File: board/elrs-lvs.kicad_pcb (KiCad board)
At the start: 4 copper layers, 46 x 22 mm, 88 parts, among them J1 PWM, J10 CF/Prog, J12 Balance, J13 U.FL, J2 PWM, J3 PWM, J4 PWM, J5 PWM, J6 PWM, J7 PWM, J8 PWM, J9 Little Tower, SW1 SW_SPST, SW2 SW_SPST, U1 ESP32-PICO-V3, U2 SX1281, U3 TPSM82901SISR, U4 2450FM07D0034T, Y1 52Mhz TCXO

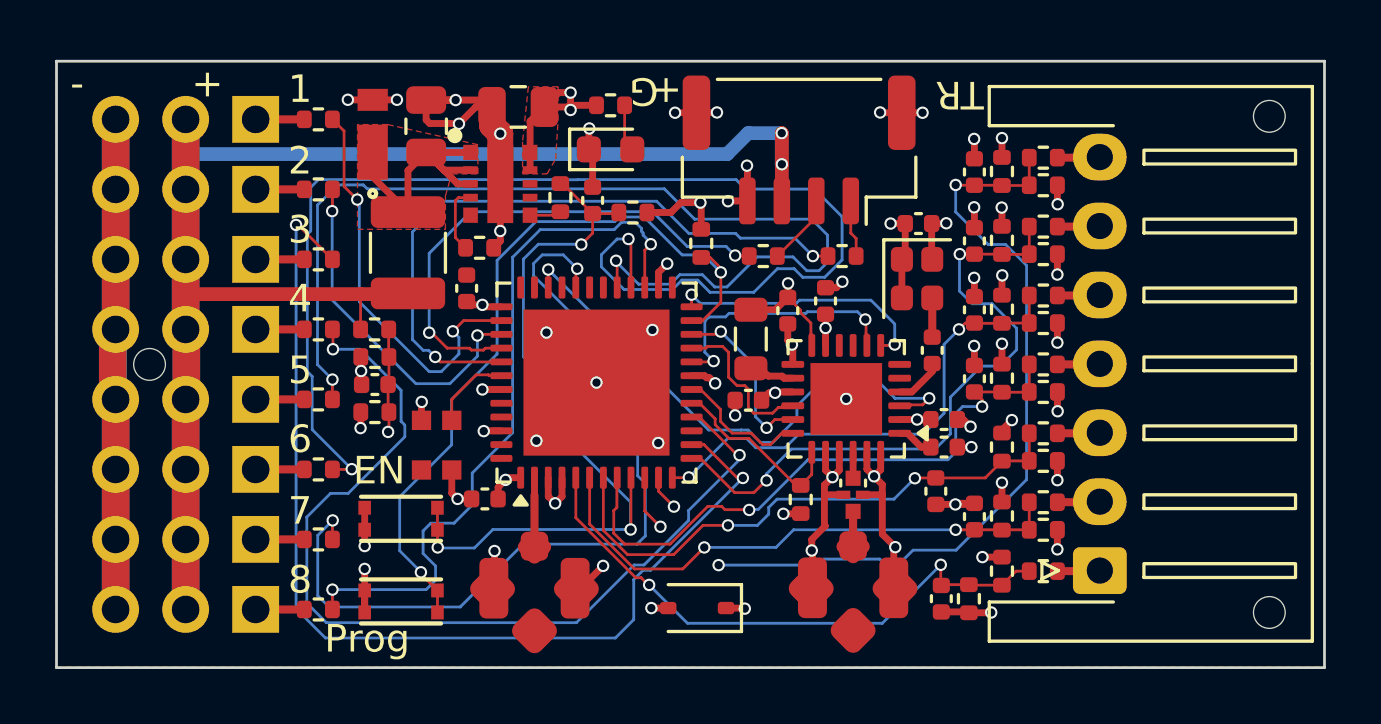
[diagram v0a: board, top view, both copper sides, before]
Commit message: modify design to use new regulator and switch part due to availability
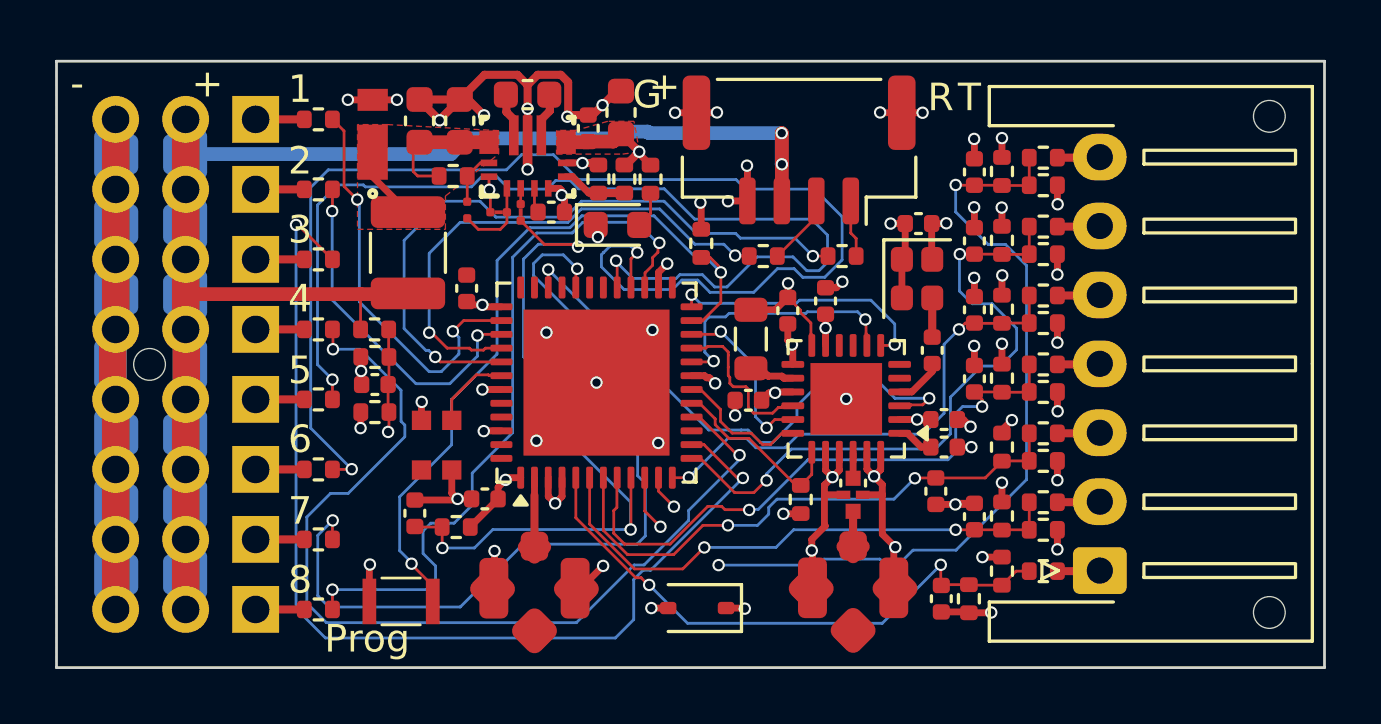
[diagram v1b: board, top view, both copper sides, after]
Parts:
- removed R2: 40.2k, Resistor_SMD:R_0402_1005Metric
- removed R3: 100, Resistor_SMD:R_0402_1005Metric
- removed SW1: SW_SPST, elrs-lvs:SO4_SW_1563-R66-8005_MIT
- removed U3: TPSM82901SISR, elrs-lvs:uSIP11_SIS_TEX
- added C22: DNP, elrs-lvs:C_0805-1206, B.Cu at (3.42, 8.46)
- added C23: 22u 25v 0603, Capacitor_SMD:C_0603_1608Metric, F.Cu at (13.2, 2.17)
- added C24: 100n, Capacitor_SMD:C_0402_1005Metric, F.Cu at (17.9, 5.47)
- added C25: >47u 0603, Capacitor_SMD:C_0603_1608Metric, F.Cu at (20.5, 1.86)
- added C27: 10u, Capacitor_SMD:C_0402_1005Metric, F.Cu at (19.3, 2.44)
- added C28: DNP, Capacitor_SMD:C_1206_3216Metric, B.Cu at (3.42, 11.0)
- added C29: DNP, elrs-lvs:C_0805-1206, B.Cu at (3.42, 13.5)
- added C30: DNP, elrs-lvs:C_0805-1206, B.Cu at (3.42, 16.1)
- added C31: DNP, elrs-lvs:C_0805-1206, B.Cu at (3.42, 18.6)
- added C5: 22u 25v 0603, Capacitor_SMD:C_0603_1608Metric, F.Cu at (14.6, 2.17)
- added JP1: JP, elrs-lvs:R_0201_0603_JP, F.Cu at (16.8, 5.49)
- added JP2: JP, elrs-lvs:R_0201_0603_JP, F.Cu at (16.0, 5.48)
- added JP3: NP, elrs-lvs:R_0201_0603_NP, F.Cu at (14.9, 5.40)
- added L2: 1-1.5uH 1A 0603, Inductor_SMD:L_0603_1608Metric, F.Cu at (17.1, 1.22)
- added R49: 470k, Resistor_SMD:R_0402_1005Metric, F.Cu at (20.6, 4.28)
- added R5: 150k, Resistor_SMD:R_0402_1005Metric, F.Cu at (19.7, 4.28)
- added R6: 10k, Resistor_SMD:R_0402_1005Metric, F.Cu at (14.4, 4.17)
- added U5: TPS63070RNMR, elrs-lvs:RNM0015A, F.Cu at (17.1, 3.46)
- C13: value 470n, 10V -> DNP; footprint Capacitor_SMD:C_0402_1005Metric -> elrs-lvs:C_0805-1206; moved to B.Cu
- C2: value 10u -> >470n; footprint Capacitor_SMD:C_0805_2012Metric -> Capacitor_SMD:C_0402_1005Metric
- C6: value 22u -> DNP; footprint Capacitor_SMD:C_0805_2012Metric -> elrs-lvs:C_0805-1206; moved to B.Cu
- SW2: footprint elrs-lvs:SO4_SW_1563-R66-8005_MIT -> elrs-lvs:SW_CK_NANOT_AS
- moved C13 23.3 mm to (3.42, 5.92), turned to 180 degrees
- moved C2 14.7 mm to (26.5, 9.05), turned to -90 degrees
- moved C6 13.4 mm to (3.42, 3.38)
- moved R1 13.1 mm to (14.5, 16.9)
- moved C1 13.1 mm to (13.0, 16.4)
- moved R14 3.05 mm to (21.6, 4.28), turned to -90 degrees
- moved D3 2.75 mm to (20.4, 5.94)
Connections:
- C13 pad 1: /V_DCC -> +5V
- C2 pad 1: VIN -> /V_DCC
- C6 pad 1: +3.3V -> +5V
- D1 pad 1: VIN -> /5V_FUSED
- F1 pad 2: VIN -> /5V_FUSED
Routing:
- net GND: track 283.5 -> 318.4 mm, vias 48 -> 52
- net VIN: track 10.7 -> 0.00 mm
- net /5V_FUSED: track 0.00 -> 7.39 mm
- net Net-(JP2-A): track 0.00 -> 2.95 mm
- net Net-(U3-MODE): track 2.46 -> 0.00 mm
- net Net-(U5-FB): track 0.00 -> 2.36 mm
- net Net-(JP3-B): track 0.00 -> 1.92 mm
- net Net-(U5-L2): track 0.00 -> 1.68 mm
- net Net-(U5-L1): track 0.00 -> 1.67 mm
- net /RESET: track 28.2 -> 27.1 mm
- net Net-(U3-PG): track 1.15 -> 0.00 mm
- net +3.3V: track 122.7 -> 121.8 mm, vias 24 -> 23
- net Net-(U5-VAUX): track 0.00 -> 0.91 mm
- net /SERIAL_TX: track 23.8 -> 24.5 mm
- net /PWM6: track 46.8 -> 47.4 mm
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- added copper zone on F.Cu, net /5V_FUSED
- removed copper zone on F.Cu, net VIN
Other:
- board text removed: "EN"

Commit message: more parts picking
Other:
- board text added: "KEM ELRS-LVS V2.1"
- board text removed: "KEM ELRS-LVS V2"

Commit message: change 17v zener to 12v - next option down from same mfr
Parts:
- C13, C22, C28, C29, C30, C31, C6: value DNP -> >16v
- D1: value 17v -> 13v
